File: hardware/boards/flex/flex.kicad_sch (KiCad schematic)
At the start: 2 parts, among them J1 Tail, J2 Tail

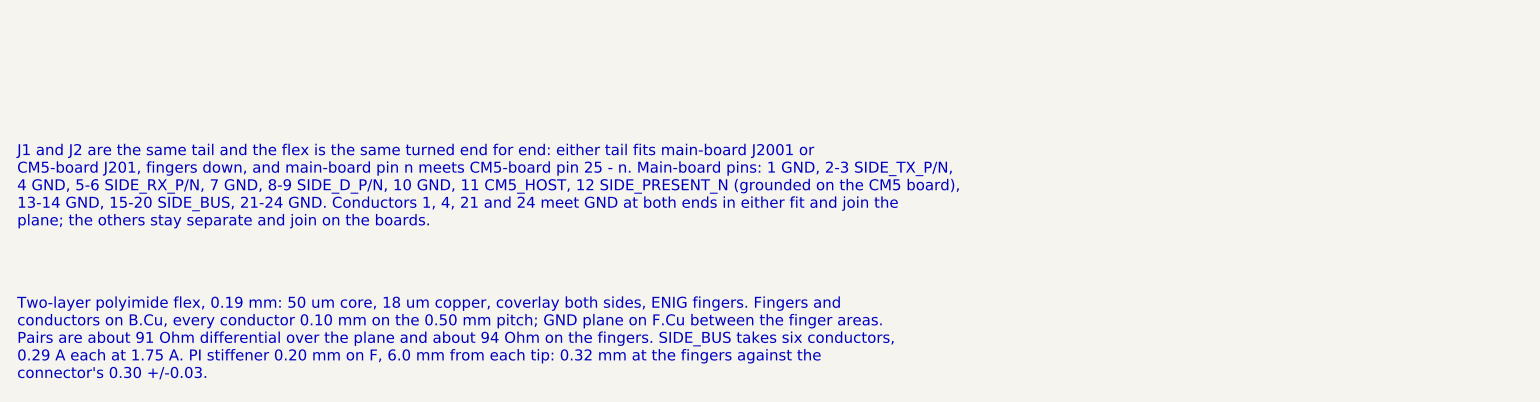
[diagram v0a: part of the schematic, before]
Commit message: feat(flex): loop the side-link flex between vertical FH12 connectors
18.4 mm end to end, fingers exposed 2.5 mm and a 0.225 mm PI stiffener to 4.2 mm from each tip (0.34 mm at the fingers against the FH12's 0.35 +/-0.03). Fitted bent 180 degrees at about 2.5 mm radius over a 1.5 mm board gap.
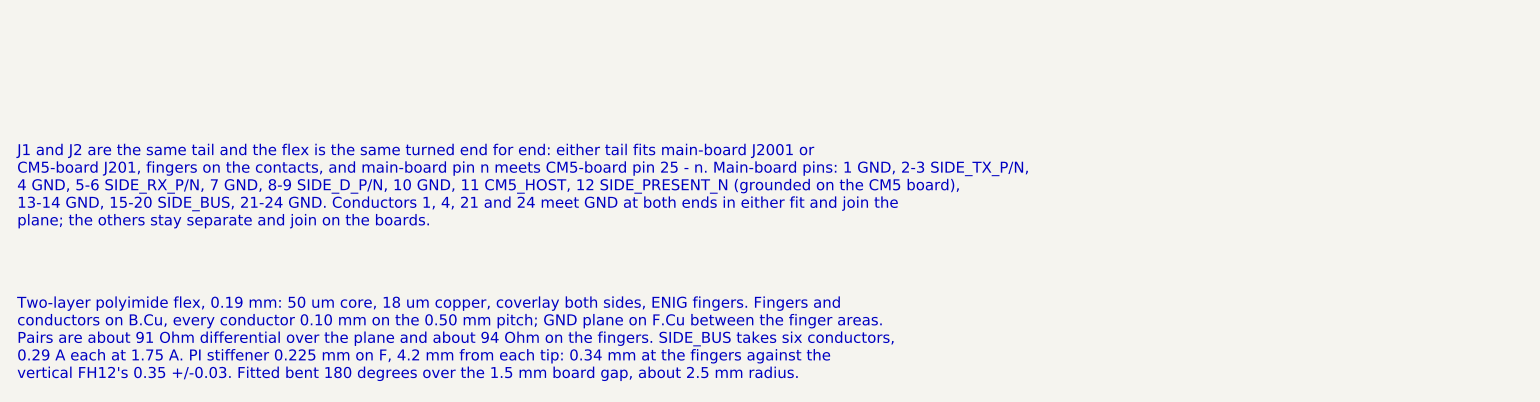
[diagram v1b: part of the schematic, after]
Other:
- note added: "J1 and J2 are the same tail and the flex is the same turned end for end: either tail fits main-board J2001 or CM5-board J201, fingers on the contacts, and main-board pin n meets CM5-board pin 25 - n. Main-board pins: 1 GND, 2-3 SIDE_TX_P/N, 4 GND, 5-6 SIDE_RX_P/N, 7 GND, 8-9 SIDE_D_P/N, 10 GND, 11 CM5_HOST, 12 SIDE_PRESENT_N (grounded on the CM5 board), 13-14 GND, 15-20 SIDE_BUS, 21-24 GND. Condu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"
- note added: "Two-layer polyimide flex, 0.19 mm: 50 um core, 18 um copper, coverlay both sides, ENIG fingers. Fingers and conductors on B.Cu, every conductor 0.10 mm on the 0.50 mm pitch; GND plane on F.Cu between the finger areas. Pairs are about 91 Ohm differential over the plane and about 94 Ohm on the fingers. SIDE_BUS takes six conductors, 0.29 A each at 1.75 A. PI stiffener 0.225 mm on F, 4.2 mm from eac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"
- note removed: "J1 and J2 are the same tail and the flex is the same turned end for end: either tail fits main-board J2001 or CM5-board J201, fingers down, and main-board pin n meets CM5-board pin 25 - n. Main-board pins: 1 GND, 2-3 SIDE_TX_P/N, 4 GND, 5-6 SIDE_RX_P/N, 7 GND, 8-9 SIDE_D_P/N, 10 GND, 11 CM5_HOST, 12 SIDE_PRESENT_N (grounded on the CM5 board), 13-14 GND, 15-20 SIDE_BUS, 21-24 GND. Conductors 1, 4,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"
- note removed: "Two-layer polyimide flex, 0.19 mm: 50 um core, 18 um copper, coverlay both sides, ENIG fingers. Fingers and conductors on B.Cu, every conductor 0.10 mm on the 0.50 mm pitch; GND plane on F.Cu between the finger areas. Pairs are about 91 Ohm differential over the plane and about 94 Ohm on the fingers. SIDE_BUS takes six conductors, 0.29 A each at 1.75 A. PI stiffener 0.20 mm on F, 6.0 mm from each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"
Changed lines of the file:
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@@
 (global_label "GND" (shape bidirectional) (at 139.7 121.92 0) (effects (font (size 1.27 1.27)) (justify left)) (property "Intersheetrefs" "${INTERSHEET_REFS}" (at 139.7 121.92 0) (hide yes) (effects (font (size 1.27 1.27)))))
 (text "Side-link flex — main board J2001 to CM5 board J201" (exclude_from_sim no) (at 25.4 20.32 0) (effects (font (size 2.54 2.54) (bold yes)) (justify left top)))
-(text "J1 and J2 are the same tail and the flex is the same turned end for end: either tail fits main-board J2001 or\nCM5-board J201, fingers down, and main-board pin n meets CM5-board pin 25 - n. Main-board pins: 1 GND, 2-3 SIDE_TX_P/N,\n4 GND, 5-6 SIDE_RX_P/N, 7 GND, 8-9 SIDE_D_P/N, 10 GND, 11 CM5_HOST, 12 SIDE_PRESENT_N (grounded on the CM5 board),\n13-14 GND, 15-20 SIDE_BUS, 21-24 GND. Conductors 1, 4, 21 and 24 meet GND at both ends in either fit and join the\nplane; the others stay separate and join on the boards." (exclude_from_sim no) (at 25.4 160.02 0) (effects (font (size 1.27 1.27)) (justify left top)))
-(text "Two-layer polyimide flex, 0.19 mm: 50 um core, 18 um copper, coverlay both sides, ENIG fingers. Fingers and\nconductors on B.Cu, every conductor 0.10 mm on the 0.50 mm pitch; GND plane on F.Cu between the finger areas.\nPairs are about 91 Ohm differential over the plane and about 94 Ohm on the fingers. SIDE_BUS takes six conductors,\n0.29 A each at 1.75 A. PI stiffener 0.20 mm on F, 6.0 mm from each tip: 0.32 mm at the fingers against the\nconnector's 0.30 +/-0.03." (exclude_from_sim no) (at 25.4 177.8 0) (effects (font (size 1.27 1.27)) (justify left top)))
+(text "J1 and J2 are the same tail and the flex is the same turned end for end: either tail fits main-board J2001 or\nCM5-board J201, fingers on the contacts, and main-board pin n meets CM5-board pin 25 - n. Main-board pins: 1 GND, 2-3 SIDE_TX_P/N,\n4 GND, 5-6 SIDE_RX_P/N, 7 GND, 8-9 SIDE_D_P/N, 10 GND, 11 CM5_HOST, 12 SIDE_PRESENT_N (grounded on the CM5 board),\n13-14 GND, 15-20 SIDE_BUS, 21-24 GND. Conductors 1, 4, 21 and 24 meet GND at both ends in either fit and join the\nplane; the others stay separate and join on the boards." (exclude_from_sim no) (at 25.4 160.02 0) (effects (font (size 1.27 1.27)) (justify left top)))
+(text "Two-layer polyimide flex, 0.19 mm: 50 um core, 18 um copper, coverlay both sides, ENIG fingers. Fingers and\nconductors on B.Cu, every conductor 0.10 mm on the 0.50 mm pitch; GND plane on F.Cu between the finger areas.\nPairs are about 91 Ohm differential over the plane and about 94 Ohm on the fingers. SIDE_BUS takes six conductors,\n0.29 A each at 1.75 A. PI stiffener 0.225 mm on F, 4.2 mm from each tip: 0.34 mm at the fingers against the\nvertical FH12's 0.35 +/-0.03. Fitted bent 180 degrees over the 1.5 mm board gap, about 2.5 mm radius." (exclude_from_sim no) (at 25.4 177.8 0) (effects (font (size 1.27 1.27)) (justify left top)))
 (sheet_instances
 		(path "/"
